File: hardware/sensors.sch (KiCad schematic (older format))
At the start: 3 parts

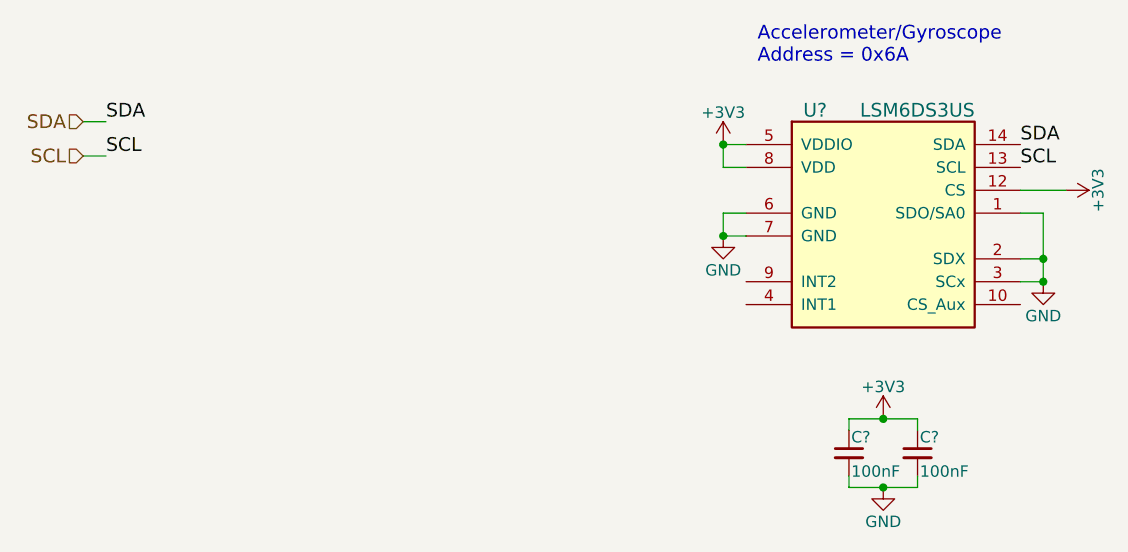
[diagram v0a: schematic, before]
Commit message: Layed board out for the third time. Doesn't include power traces yet.
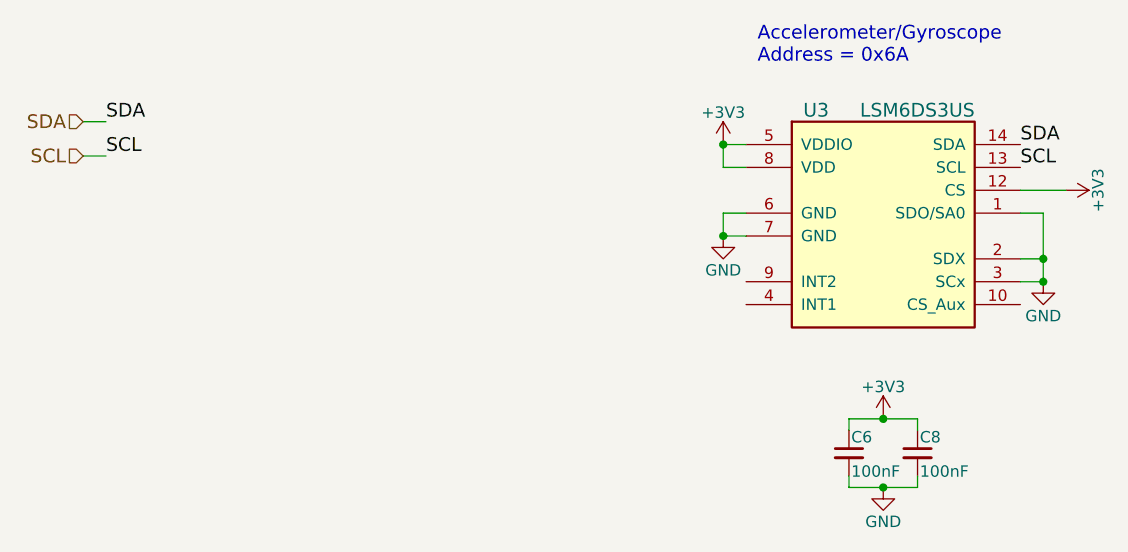
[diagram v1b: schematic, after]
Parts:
- U3: renamed from U?; footprint modules:LSM6DS3US -> parts:LSM6DS3US
- gave numbers to parts that had none: 2
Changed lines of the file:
@@
 EESchema Schematic File Version 2
+LIBS:power
+LIBS:device
+LIBS:transistors
+LIBS:conn
+LIBS:linear
+LIBS:regul
+LIBS:74xx
+LIBS:cmos4000
+LIBS:adc-dac
+LIBS:memory
+LIBS:xilinx
+LIBS:microcontrollers
+LIBS:dsp
+LIBS:microchip
+LIBS:analog_switches
+LIBS:motorola
+LIBS:texas
+LIBS:intel
+LIBS:audio
+LIBS:interface
+LIBS:digital-audio
+LIBS:philips
+LIBS:display
+LIBS:cypress
+LIBS:siliconi
+LIBS:opto
+LIBS:atmel
+LIBS:contrib
+LIBS:valves
+LIBS:stm32
+LIBS:switches
 LIBS:parts
 LIBS:minibot-cache
@@
 $Descr A4 11693 8268
 encoding utf-8
-Sheet 4 5
+Sheet 4 4
 Title ""
 Date ""
@@
 $EndDescr
 $Comp
-L C_Small C?
+L C_Small C6
 U 1 1 59A5481E
 P 5700 4750
-F 0 "C?" H 5710 4820 50  0000 L CNN
+F 0 "C6" H 5710 4820 50  0000 L CNN
 F 1 "100nF" H 5710 4670 50  0000 L CNN
 F 2 "Capacitors_SMD:C_0603" H 5700 4750 50  0001 C CNN
@@
 $EndComp
 $Comp
-L GND #PWR?
+L GND #PWR045
 U 1 1 59A54825
 P 5850 4900
-F 0 "#PWR?" H 5850 4650 50  0001 C CNN
+F 0 "#PWR045" H 5850 4650 50  0001 C CNN
 F 1 "GND" H 5850 4750 50  0000 C CNN
 F 2 "" H 5850 4900 50  0001 C CNN
@@
 $EndComp
 $Comp
-L LSM6DS3US U?
+L LSM6DS3US U3
 U 1 1 59A5482B
 P 5450 3300
-F 0 "U?" H 5500 3350 60  0000 L CNN
+F 0 "U3" H 5500 3350 60  0000 L CNN
 F 1 "LSM6DS3US" H 6250 3350 60  0000 R CNN
-F 2 "modules:LSM6DS3US" H 5450 3300 60  0001 C CNN
+F 2 "parts:LSM6DS3US" H 5450 3300 60  0001 C CNN
 F 3 "" H 5450 3300 60  0001 C CNN
 	1    5450 3300
@@
 $EndComp
 $Comp
-L GND #PWR?
+L GND #PWR046
 U 1 1 59A54832
 P 5150 3800
-F 0 "#PWR?" H 5150 3550 50  0001 C CNN
+F 0 "#PWR046" H 5150 3550 50  0001 C CNN
 F 1 "GND" H 5150 3650 50  0000 C CNN
 F 2 "" H 5150 3800 50  0001 C CNN
@@
 Connection ~ 5150 3400
 $Comp
-L C_Small C?
+L C_Small C8
 U 1 1 59A54840
 P 6000 4750
-F 0 "C?" H 6010 4820 50  0000 L CNN
+F 0 "C8" H 6010 4820 50  0000 L CNN
 F 1 "100nF" H 6010 4670 50  0000 L CNN
 F 2 "Capacitors_SMD:C_0603" H 6000 4750 50  0001 C CNN
@@
 Connection ~ 5850 4600
 $Comp
-L GND #PWR?
+L GND #PWR047
 U 1 1 59A54851
 P 6550 4000
-F 0 "#PWR?" H 6550 3750 50  0001 C CNN
+F 0 "#PWR047" H 6550 3750 50  0001 C CNN
 F 1 "GND" H 6550 3850 50  0000 C CNN
 F 2 "" H 6550 4000 50  0001 C CNN
@@
 SCL
 $Comp
-L +3V3 #PWR?
+L +3V3 #PWR048
 U 1 1 59A54862
 P 6650 3600
-F 0 "#PWR?" H 6650 3450 50  0001 C CNN
+F 0 "#PWR048" H 6650 3450 50  0001 C CNN
 F 1 "+3V3" H 6650 3740 50  0000 C CNN
 F 2 "" H 6650 3600 50  0001 C CNN
@@
 $EndComp
 $Comp
-L +3V3 #PWR?
+L +3V3 #PWR049
 U 1 1 59A54868
 P 5150 3400
-F 0 "#PWR?" H 5150 3250 50  0001 C CNN
+F 0 "#PWR049" H 5150 3250 50  0001 C CNN
 F 1 "+3V3" H 5150 3540 50  0000 C CNN
 F 2 "" H 5150 3400 50  0001 C CNN
@@
 $EndComp
 $Comp
-L +3V3 #PWR?
+L +3V3 #PWR050
 U 1 1 59A5486E
 P 5850 4600
-F 0 "#PWR?" H 5850 4450 50  0001 C CNN
+F 0 "#PWR050" H 5850 4450 50  0001 C CNN
 F 1 "+3V3" H 5850 4740 50  0000 C CNN
 F 2 "" H 5850 4600 50  0001 C CNN
